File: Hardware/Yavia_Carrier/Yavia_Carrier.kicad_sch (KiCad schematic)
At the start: 58 parts, among them J1 Power, J10 52610-1572, J2 Serial, J3 STRB_IS, J4 STRB_IS, J5 STRB, J6 STRB, J7 52610-1572, J8 FLASH, J9 FLASH, Q1 MMBT2222ALT1G, Q2 MMBT2222ALT1G, U1 Verdin iMX8M Plus, U2 AP63203, U3 LM3671, U4 TCMT1103, U5 TCMT1103, U6 LDD600L, U7 LDD600L, U8 74AHC1G32, U9 74AHC1G32

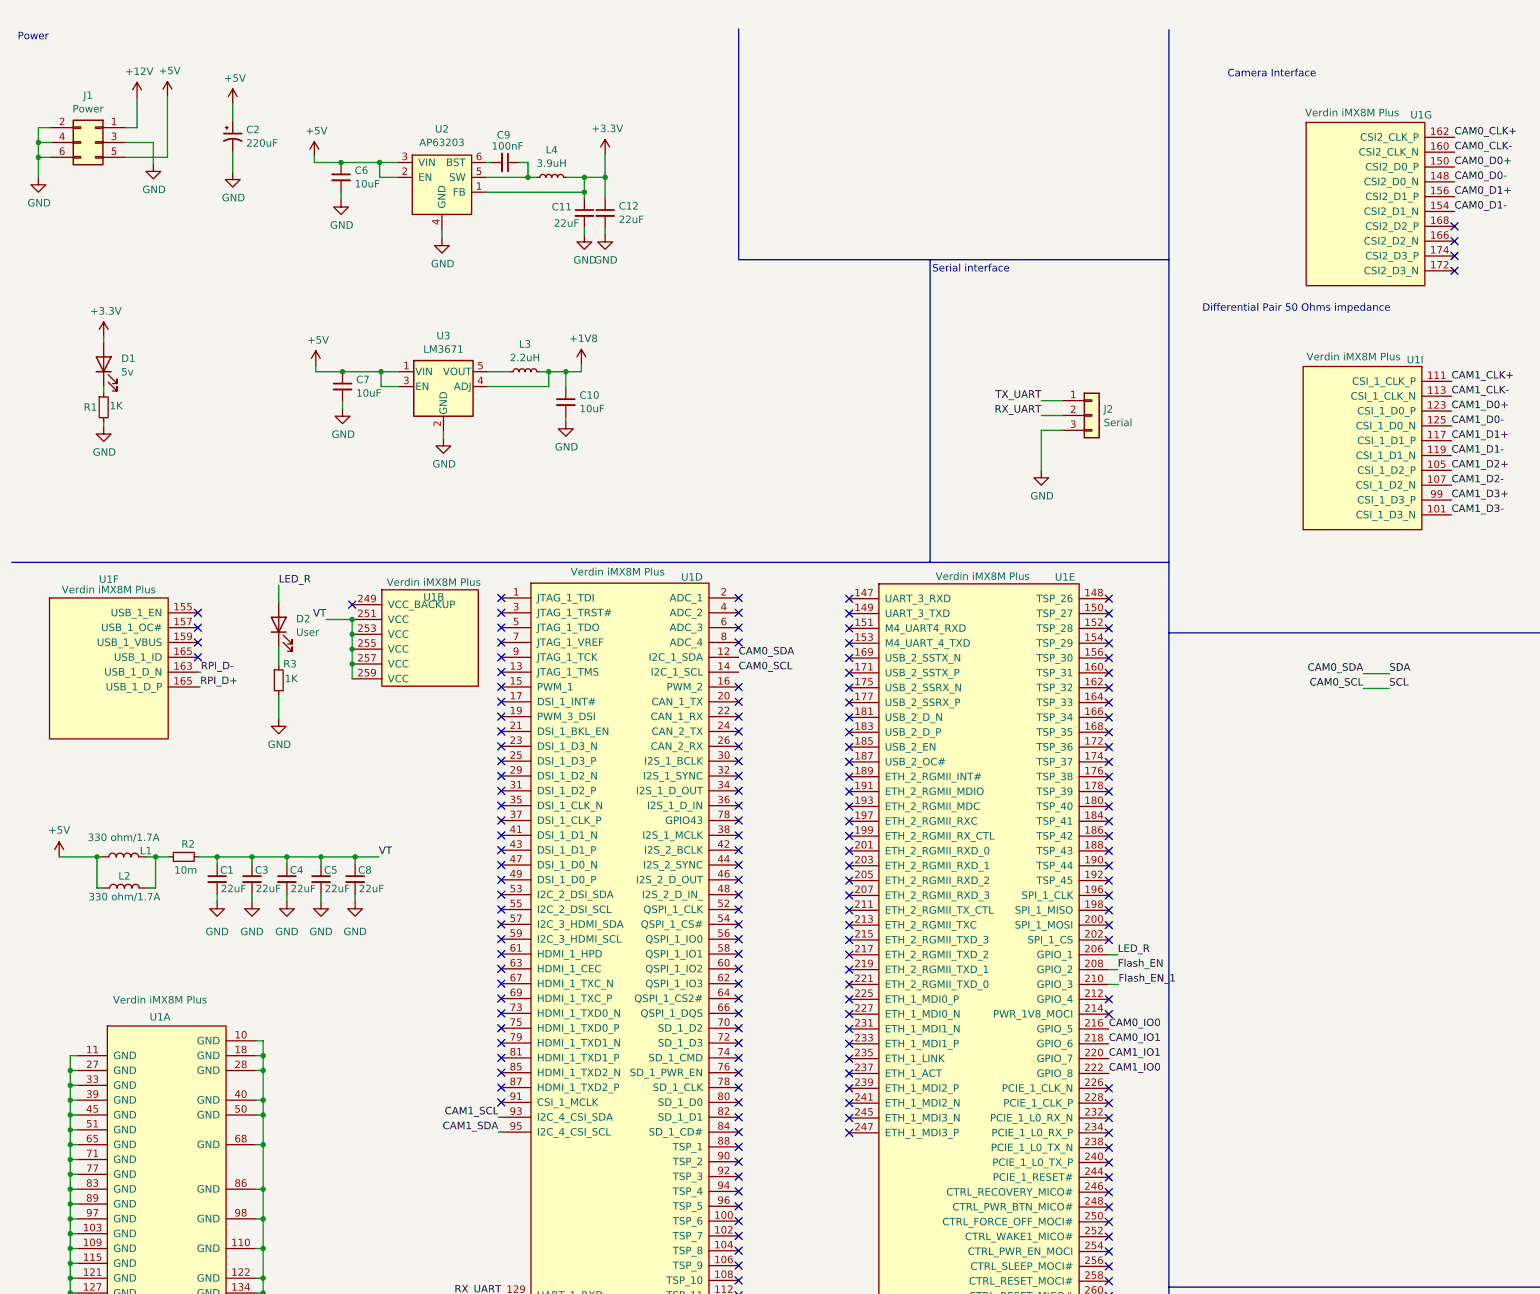
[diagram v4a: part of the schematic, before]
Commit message: start of component arrangement & add 3d models
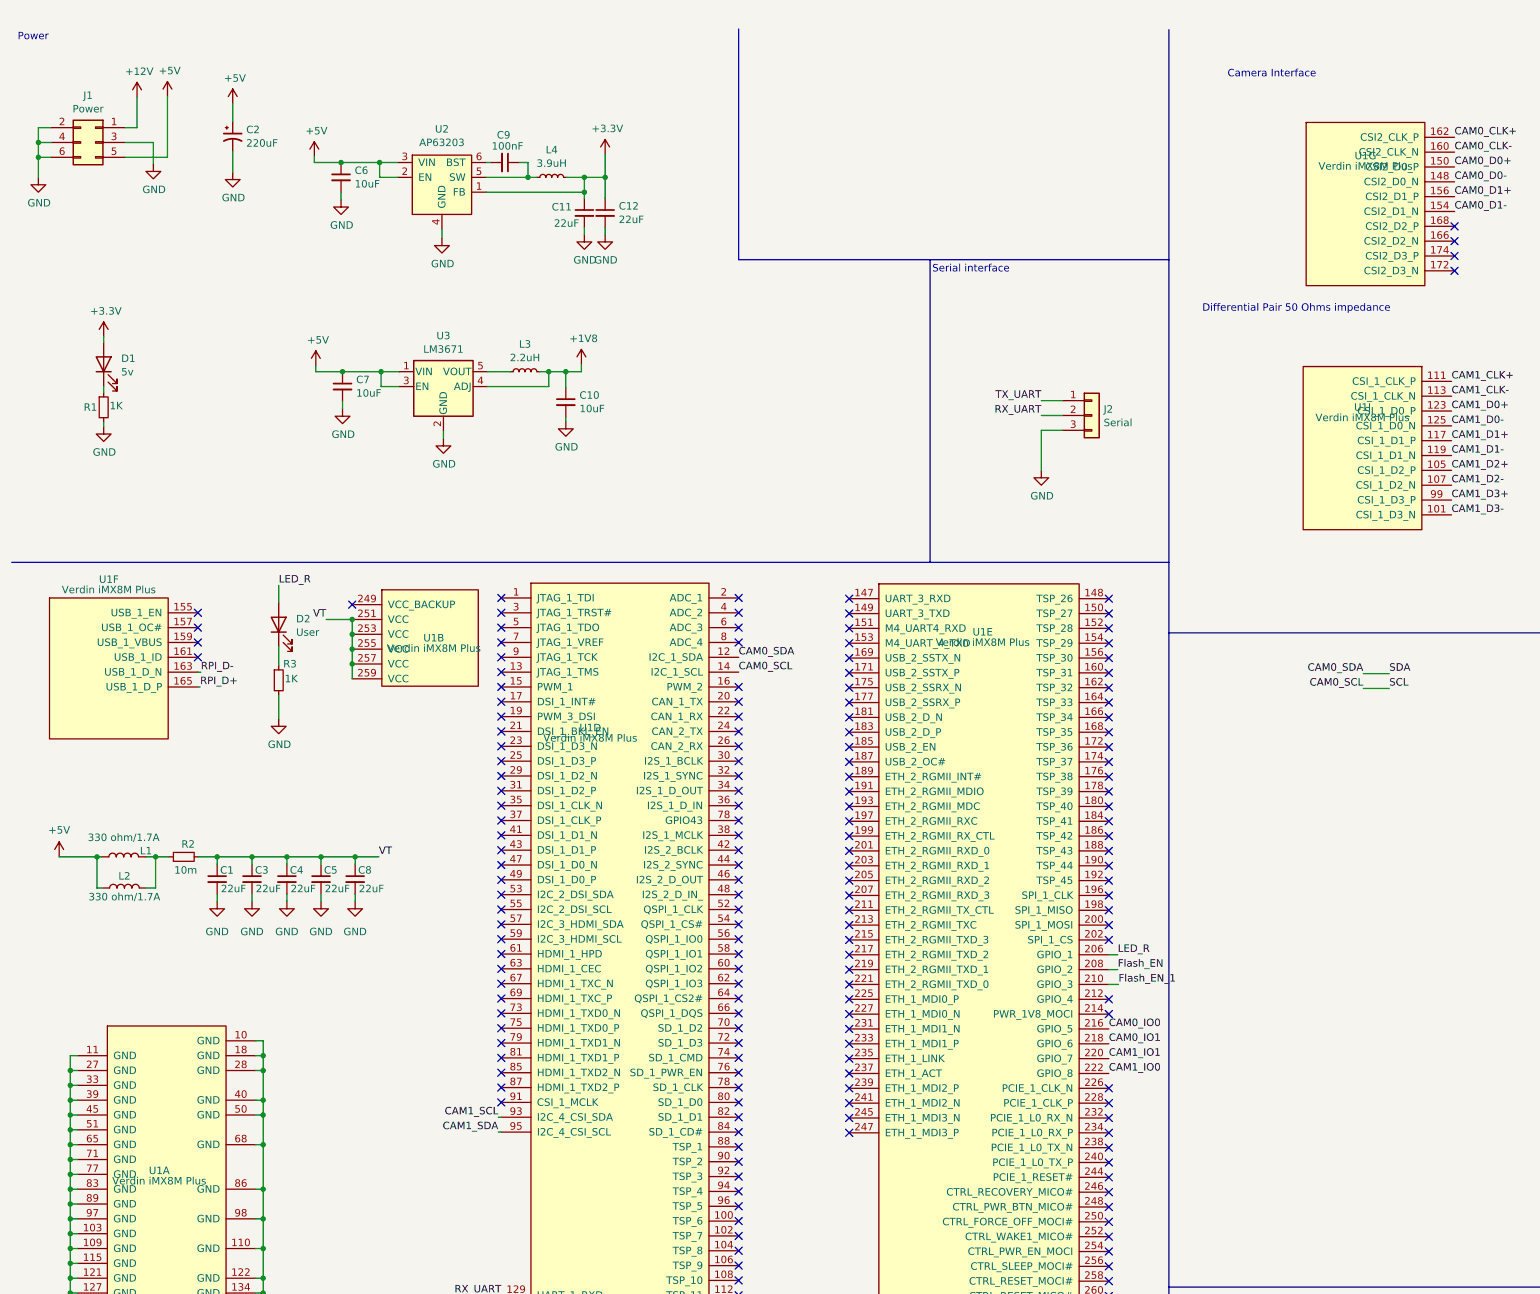
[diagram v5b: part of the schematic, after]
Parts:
- L1, L2: footprint (none) -> Inductor_SMD:L_0603_1608Metric; Campo4 (none) -> MPZ1608S331ATA00
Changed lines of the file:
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@@
   (symbol (lib_name "Yavia_carrier_10") (lib_id "Verdin iMX8M Plus:Yavia_carrier") (at 243.713 41.91 0) (unit 7)
     (in_bom yes) (on_board yes) (dnp no)
-    (property "Reference" "U1" (at 253.238 26.67 0)
+    (property "Reference" "U1" (at 243.713 33.655 0)
       (effects (font (size 1.27 1.27)))
     )
-    (property "Value" "Verdin iMX8M Plus" (at 241.427 26.289 0)
+    (property "Value" "Verdin iMX8M Plus" (at 243.713 35.433 0)
       (effects (font (size 1.27 1.27)))
     )
@@
     (pin "163")
     (pin "165")
-    (pin "165")
+    (pin "161")
     (pin "148")
     (pin "150")
@@
       (effects (font (size 1.27 1.27)))
     )
-    (property "Footprint" "" (at 31.115 153.67 0)
+    (property "Footprint" "Inductor_SMD:L_0603_1608Metric" (at 31.115 153.67 0)
       (effects (font (size 1.27 1.27)) hide)
     )
@@
       (effects (font (size 1.27 1.27)) hide)
     )
+    (property "Campo4" "MPZ1608S331ATA00" (at 31.115 153.67 90)
+      (effects (font (size 1.27 1.27)) hide)
+    )
     (pin "1")
     (pin "2")
@@
   (symbol (lib_name "Yavia_carrier_6") (lib_id "Verdin iMX8M Plus:Yavia_carrier") (at 37.211 215.646 0) (unit 1)
     (in_bom yes) (on_board yes) (dnp no)
-    (property "Reference" "U1" (at 37.338 181.102 0)
+    (property "Reference" "U1" (at 37.211 207.391 0)
       (effects (font (size 1.27 1.27)))
     )
-    (property "Value" "Verdin iMX8M Plus" (at 37.338 178.181 0)
+    (property "Value" "Verdin iMX8M Plus" (at 37.211 209.169 0)
       (effects (font (size 1.27 1.27)))
     )
@@
     (pin "163")
     (pin "165")
-    (pin "165")
+    (pin "161")
     (pin "148")
     (pin "150")
@@
   (symbol (lib_name "Yavia_carrier_5") (lib_id "Verdin iMX8M Plus:Yavia_carrier") (at 178.181 123.444 0) (unit 5)
     (in_bom yes) (on_board yes) (dnp no)
-    (property "Reference" "U1" (at 192.278 105.791 0)
+    (property "Reference" "U1" (at 178.181 115.189 0)
       (effects (font (size 1.27 1.27)))
     )
-    (property "Value" "Verdin iMX8M Plus" (at 178.181 105.664 0)
+    (property "Value" "Verdin iMX8M Plus" (at 178.181 116.967 0)
       (effects (font (size 1.27 1.27)))
     )
@@
     (pin "163")
     (pin "165")
-    (pin "165")
+    (pin "161")
     (pin "148")
     (pin "150")
@@
   (symbol (lib_name "Yavia_carrier_8") (lib_id "Verdin iMX8M Plus:Yavia_carrier") (at 243.205 84.963 0) (unit 9)
     (in_bom yes) (on_board yes) (dnp no)
-    (property "Reference" "U1" (at 252.222 68.58 0)
+    (property "Reference" "U1" (at 243.205 76.708 0)
       (effects (font (size 1.27 1.27)))
     )
-    (property "Value" "Verdin iMX8M Plus" (at 241.681 68.072 0)
+    (property "Value" "Verdin iMX8M Plus" (at 243.205 78.486 0)
       (effects (font (size 1.27 1.27)))
     )
@@
     (pin "163")
     (pin "165")
-    (pin "165")
+    (pin "161")
     (pin "148")
     (pin "150")
@@
       (effects (font (size 1.27 1.27)))
     )
-    (property "Footprint" "" (at 31.242 159.004 0)
+    (property "Footprint" "Inductor_SMD:L_0603_1608Metric" (at 31.242 159.004 0)
       (effects (font (size 1.27 1.27)) hide)
     )
@@
       (effects (font (size 1.27 1.27)) hide)
     )
+    (property "Campo4" "MPZ1608S331ATA00" (at 31.242 159.004 90)
+      (effects (font (size 1.27 1.27)) hide)
+    )
     (pin "1")
     (pin "2")
@@
     (pin "163")
     (pin "165")
-    (pin "165")
+    (pin "161")
     (pin "148")
     (pin "150")
@@
   (symbol (lib_name "Yavia_carrier_2") (lib_id "Verdin iMX8M Plus:Yavia_carrier") (at 84.201 124.46 0) (unit 2)
     (in_bom yes) (on_board yes) (dnp no)
-    (property "Reference" "U1" (at 84.201 109.22 0)
+    (property "Reference" "U1" (at 84.201 116.205 0)
       (effects (font (size 1.27 1.27)))
     )
-    (property "Value" "Verdin iMX8M Plus" (at 84.201 106.68 0)
+    (property "Value" "Verdin iMX8M Plus" (at 84.201 117.983 0)
       (effects (font (size 1.27 1.27)))
     )
@@
     (pin "163")
     (pin "165")
-    (pin "165")
+    (pin "161")
     (pin "148")
     (pin "150")
@@
   (symbol (lib_name "Yavia_carrier_1") (lib_id "Verdin iMX8M Plus:Yavia_carrier") (at 110.998 139.827 0) (unit 4)
     (in_bom yes) (on_board yes) (dnp no)
-    (property "Reference" "U1" (at 128.397 105.791 0)
+    (property "Reference" "U1" (at 110.998 131.572 0)
       (effects (font (size 1.27 1.27)))
     )
-    (property "Value" "Verdin iMX8M Plus" (at 115.697 104.902 0)
+    (property "Value" "Verdin iMX8M Plus" (at 110.998 133.35 0)
       (effects (font (size 1.27 1.27)))
     )
@@
     (pin "163")
     (pin "165")
-    (pin "165")
+    (pin "161")
     (pin "148")
     (pin "150")
